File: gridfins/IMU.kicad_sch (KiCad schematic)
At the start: 11 parts, among them U7 ICM-20608-G, U8 MMC5983MA, U9 H3LIS331DLTR

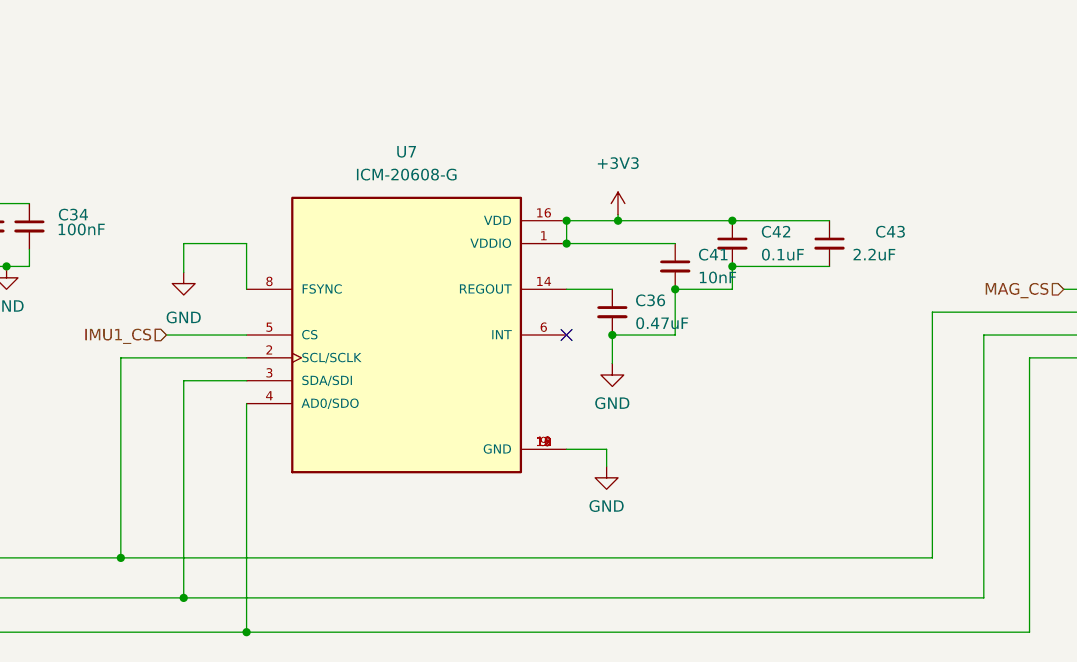
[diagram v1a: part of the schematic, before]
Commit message: deleted obsolete ICM-20608-G from IMU, added WSEN-ISDS adviced by Jack, a 6 axis IMU. Added footprint and symbol. Yet to finish connections and finish the "application circuit". Added footprint for 6pin connector in Linear Actuator sheet.
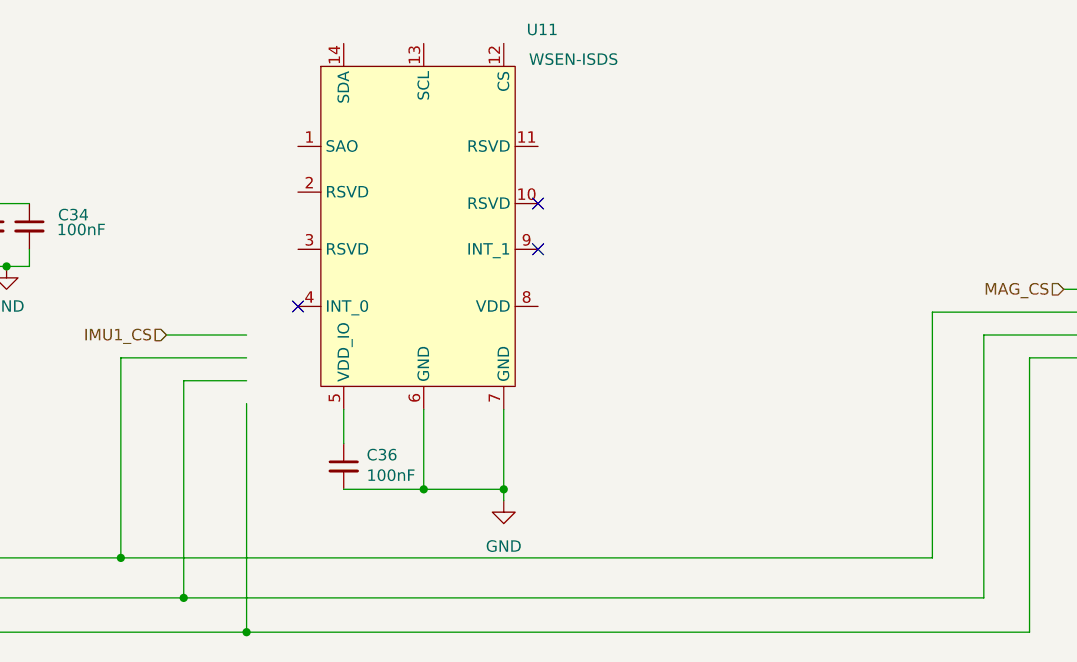
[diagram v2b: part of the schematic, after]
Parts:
- removed C41: 10nF, Capacitor_SMD:C_0402_1005Metric, symbol Device:C_Small
- removed C42: 0.1uF, Capacitor_SMD:C_0402_1005Metric, symbol Device:C_Small
- removed C43: 2.2uF, Capacitor_SMD:C_0402_1005Metric, symbol Device:C_Small
- removed U7: ICM-20608-G, iclr:PQFN50P300X300X80-16N, symbol iclr:ICM-20608-G
- added U11: WSEN-ISDS, iclr:PQFN50P300X300X80-16N, symbol iclr:WSEN_ISDS
- C36: value 0.47uF -> 100nF; footprint Capacitor_SMD:C_0402_1005Metric -> (none)
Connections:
- net GND: now also U11.6 (GND), U11.7 (GND)
- net at C36.1: now also U11.5 (VDD_IO)
- no-connect marks 4 -> 6

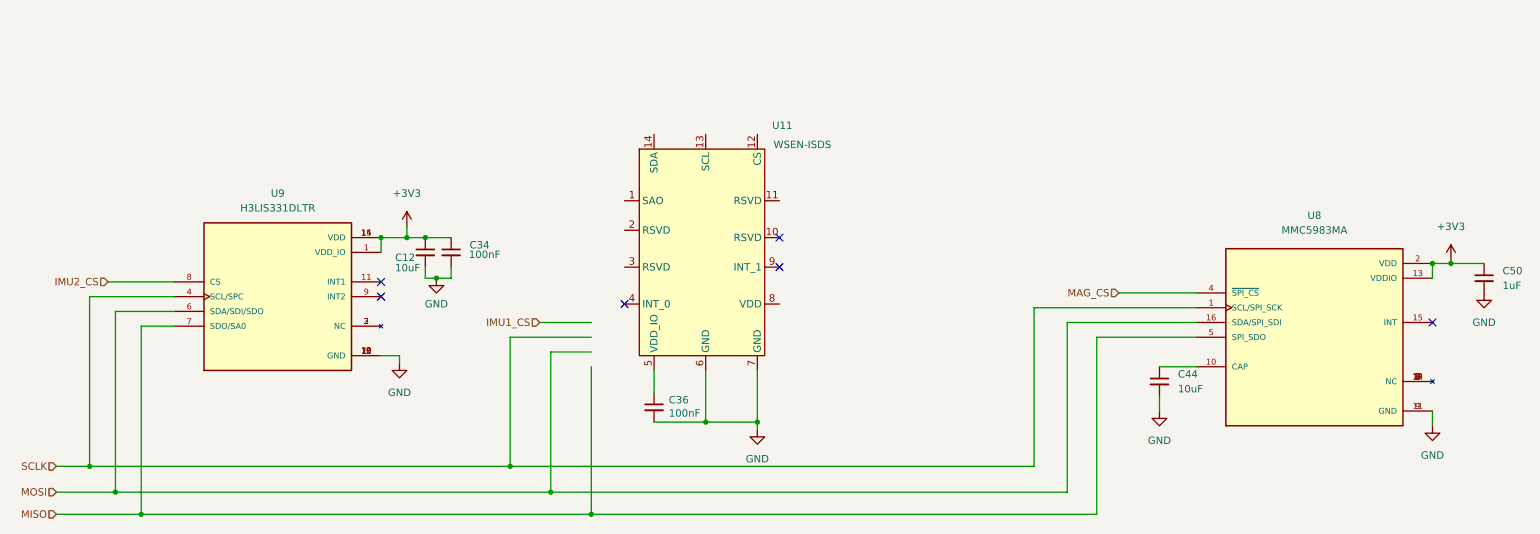
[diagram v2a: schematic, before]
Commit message: IMU replacement
created symbol and completed operational circuit for the WSEN-IDS 6 axis imu chip. Chip select accessed through the same - IMU1_CS. Need to verify direction of SCL port
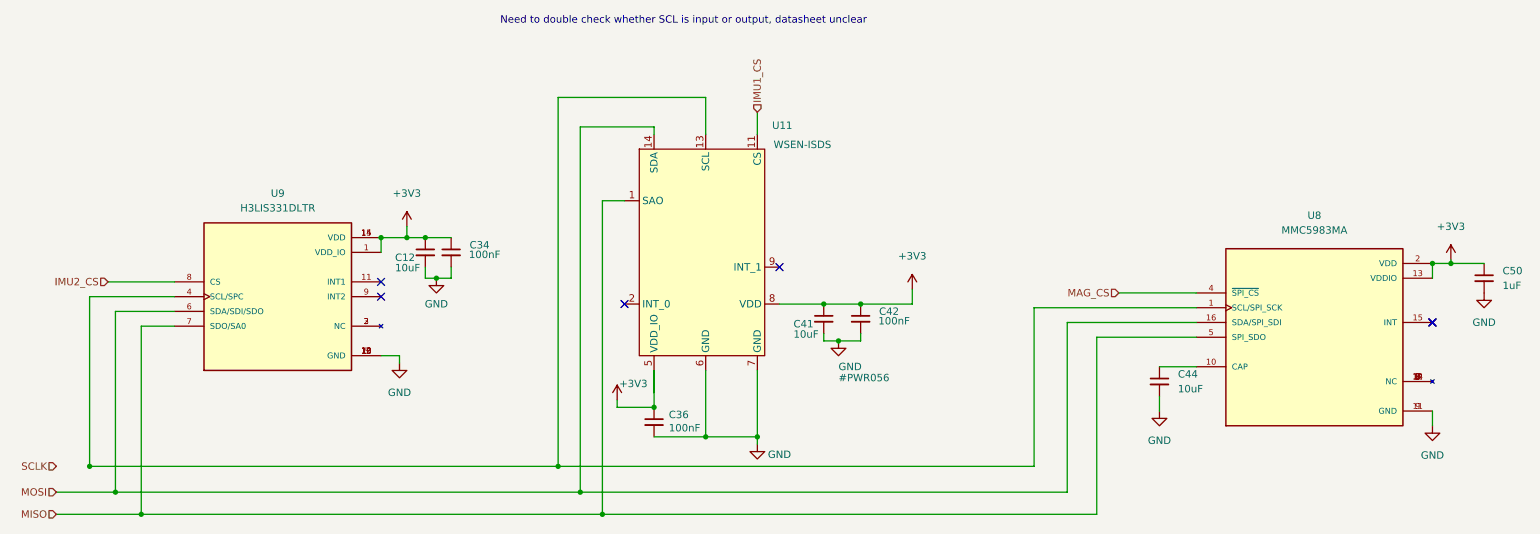
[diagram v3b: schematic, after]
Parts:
- added C41: 10uF, Capacitor_SMD:C_0402_1005Metric, symbol Device:C_Small
- added C42: 100nF, Capacitor_SMD:C_0402_1005Metric, symbol Device:C_Small
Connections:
- net +3V3: now also C36.1, U11.5 (VDD_IO), U11.8 (VDD), C41.1, C42.1
- net GND: now also C41.2, C42.2
- net IMU1_CS: now also U11.11 (CS)
- net MISO: now also U11.1 (SAO)
- net MOSI: now also U11.14 (SDA)
- net SCLK: no longer U8.1 (SCL/SPI_SCK), U9.4 (SCL/SPC)
- net at U11.13 (SCL): now also U8.1 (SCL/SPI_SCK), U9.4 (SCL/SPC)
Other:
- note added: "Need to double check whether SCL is input or output, datasheet unclear"
- moved on the sheet: C36

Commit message: Imported Official footprints and symbol
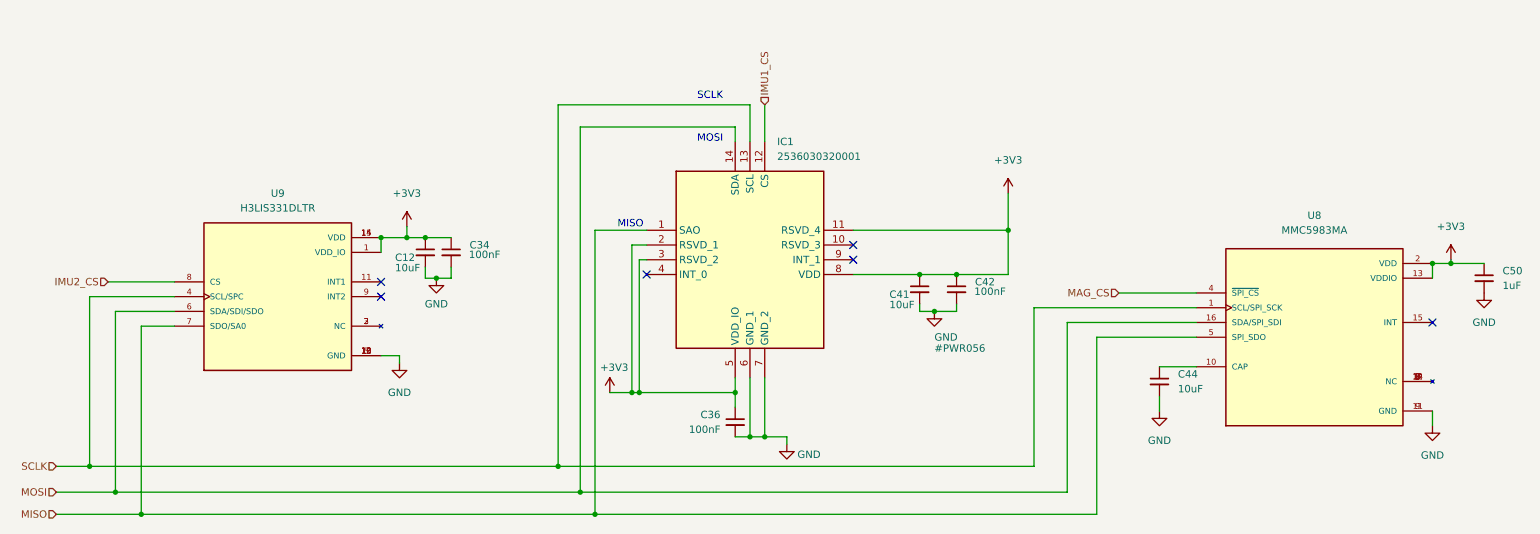
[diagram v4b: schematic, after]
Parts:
- removed U11: WSEN-ISDS, iclr:PQFN50P300X300X80-16N, symbol iclr:WSEN_ISDS
- added IC1: 2536030320001, 2536030320001, symbol iclr:2536030320001
- C36: footprint (none) -> Capacitor_SMD:C_0402_1005Metric
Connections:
- net +3V3: now also IC1.11 (RSVD_4), IC1.2 (RSVD_1), IC1.3 (RSVD_2), IC1.5 (VDD_IO), IC1.8 (VDD)
- net GND: now also IC1.6 (GND_1), IC1.7 (GND_2)
- net IMU1_CS: now also IC1.12 (CS)
- net MISO: now also IC1.1 (SAO)
- net MOSI: now also IC1.14 (SDA)
- net SCLK: now also U8.1 (SCL/SPI_SCK), U9.4 (SCL/SPC), IC1.13 (SCL)
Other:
- note added: "MISO"
- note added: "MOSI"
- note added: "SCLK"
- note removed: "Need to double check whether SCL is input or output, datasheet unclear"
- moved on the sheet: C41, C42

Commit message: buck PCB
progress - starting from buck converter STEP 4
- Rboot ad Cboot placed near the chip and between pin 23 and 24. Both capcitor and resistor of the recommended size 0402

moved snubber up to top layer

began to move
analog components to left side while power components to right of IC
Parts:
- IC1: footprint 2536030320001 -> iclr:2536030320001
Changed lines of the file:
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@@
 			)
 		)
-		(property "Footprint" "2536030320001"
+		(property "Footprint" "iclr:2536030320001"
 			(at 161.29 144.45 0)
 			(effects
